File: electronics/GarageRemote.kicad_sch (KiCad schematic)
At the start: 33 parts, among them J1 CC1101 Module, J2 SERIAL, J3 ICSP, U1 TXS0108EPW, U2 ATmega328P-A, U3 MAX7060ATGT, Y1 16MHz, Y2 14.318MHz

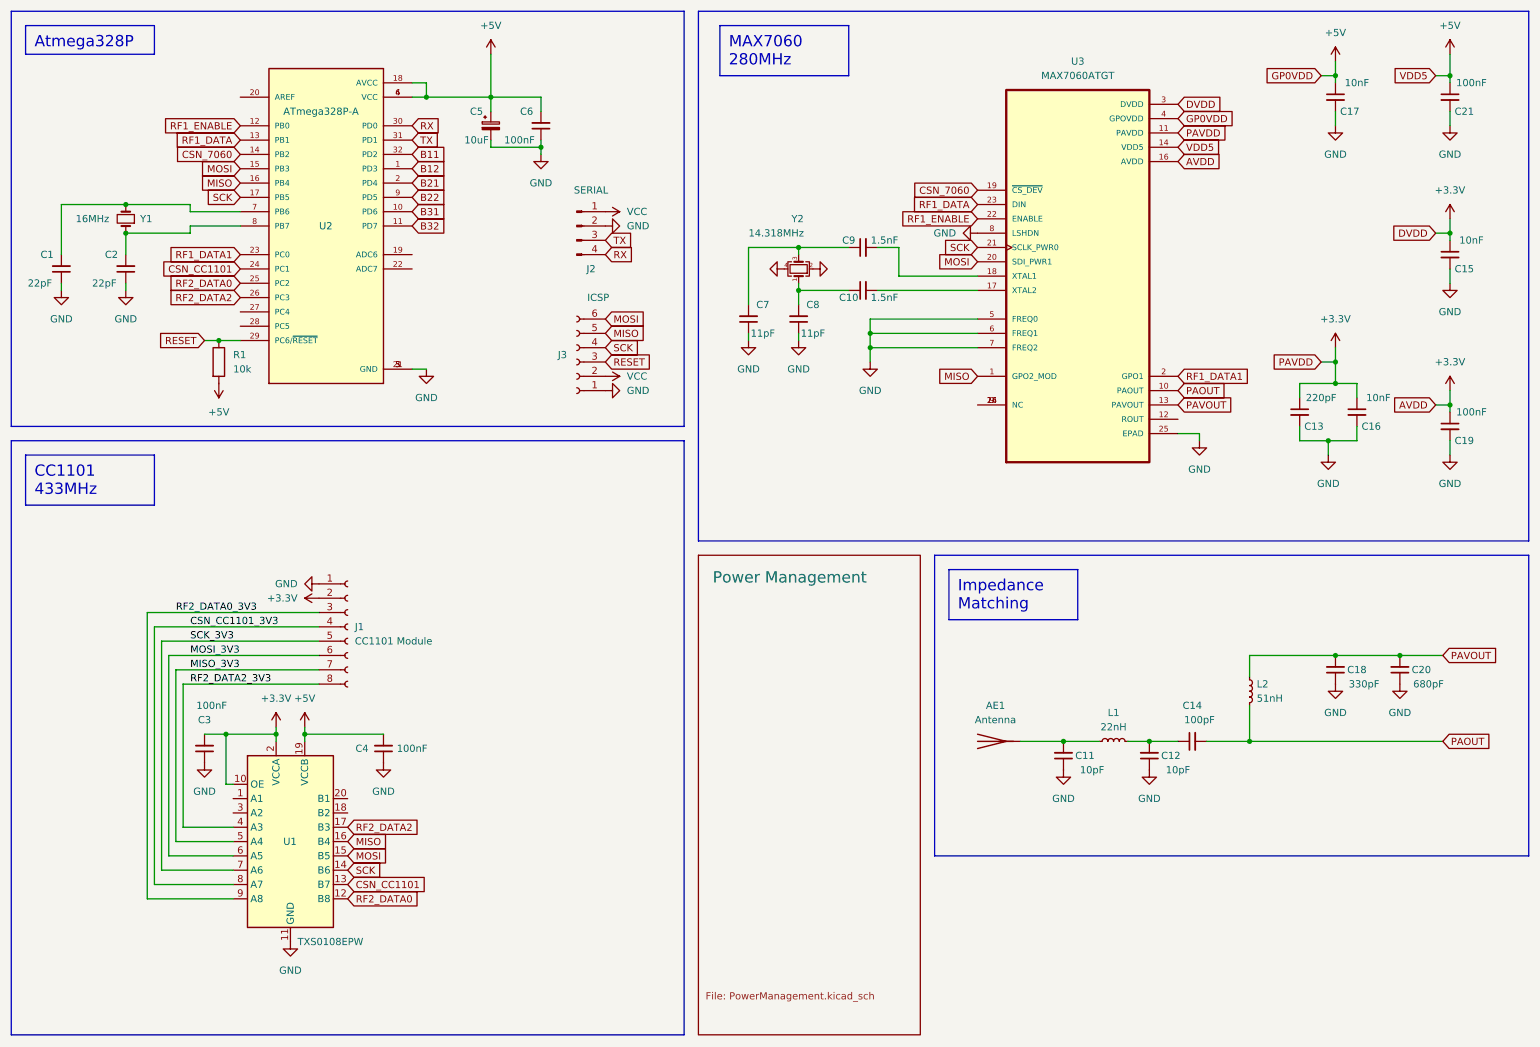
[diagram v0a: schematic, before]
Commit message: Fix & simplify schematic
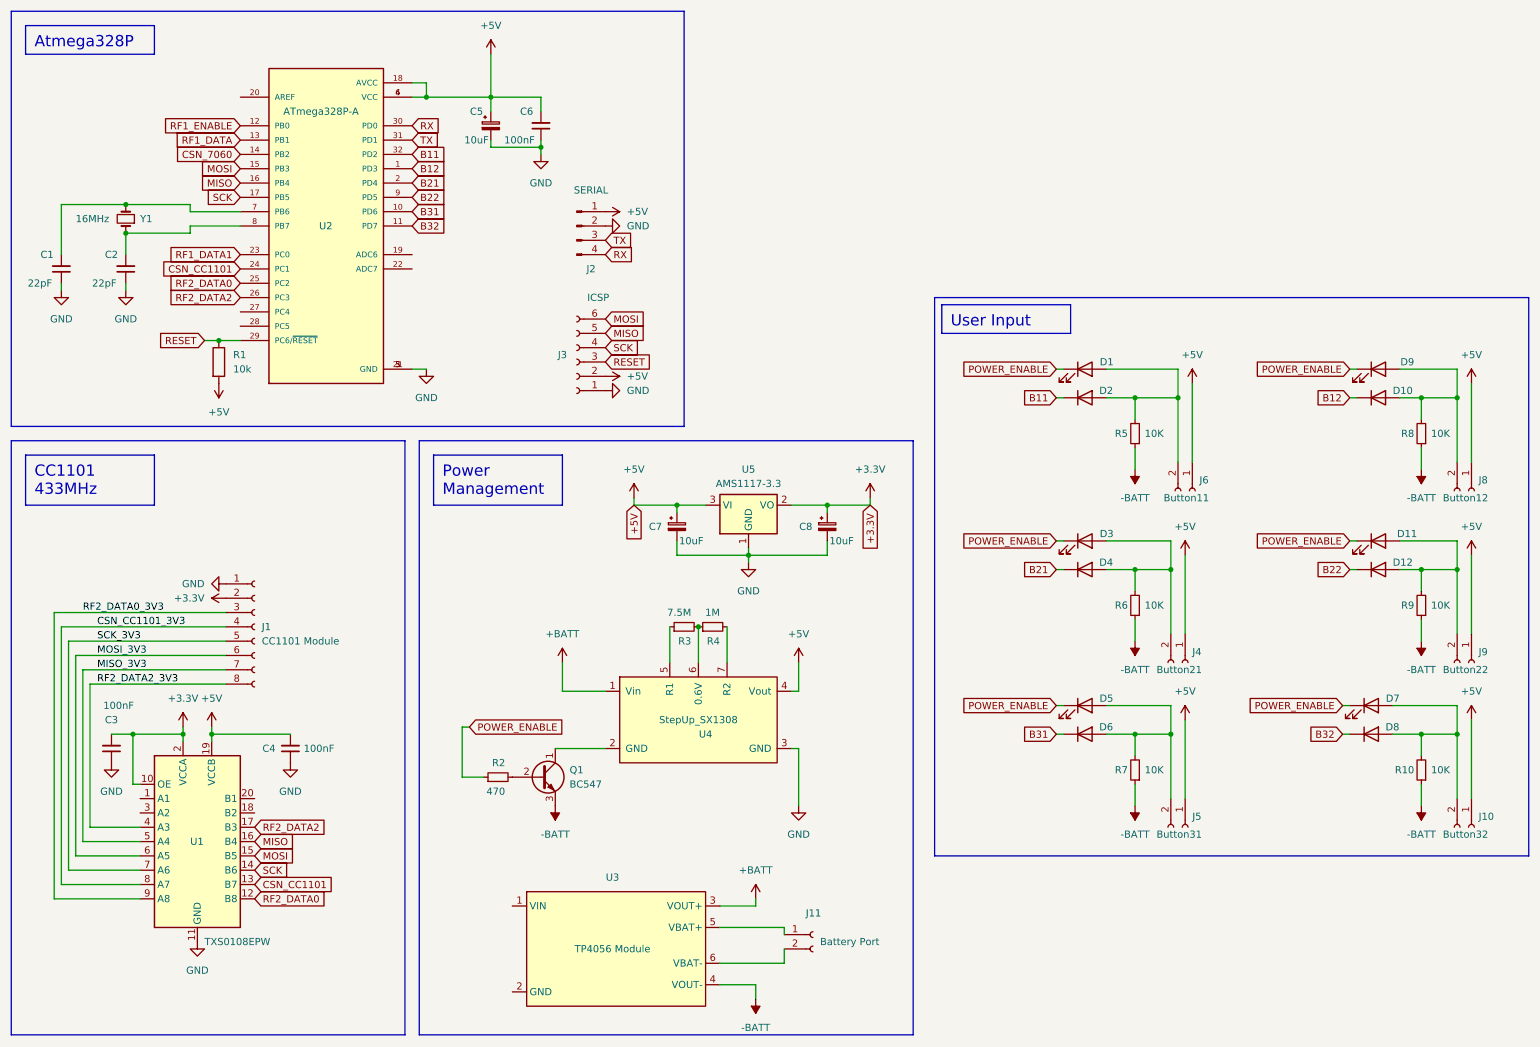
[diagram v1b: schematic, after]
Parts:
- removed AE1: Antenna, AA_Footprints:SMA-J-P-X-ST-EM1_EdgeMount, symbol Device:Antenna
- removed C10, C9: 1.5nF, Capacitor_SMD:C_0805_2012Metric_Pad1.18x1.45mm_HandSolder, symbol Device:C_Small
- removed C11, C12: 10pF, Capacitor_SMD:C_0805_2012Metric_Pad1.18x1.45mm_HandSolder, symbol Device:C_Small
- removed C13: 220pF, Capacitor_SMD:C_0805_2012Metric_Pad1.18x1.45mm_HandSolder, symbol Device:C_Small
- removed C14: 100pF, Capacitor_SMD:C_0805_2012Metric_Pad1.18x1.45mm_HandSolder, symbol Device:C_Small
- removed C15, C16, C17: 10nF, Capacitor_SMD:C_0805_2012Metric_Pad1.18x1.45mm_HandSolder, symbol Device:C_Small
- removed C18: 330pF, Capacitor_SMD:C_0805_2012Metric_Pad1.18x1.45mm_HandSolder, symbol Device:C_Small
- removed C19, C21: 100nF, Capacitor_SMD:C_1210_3225Metric_Pad1.33x2.70mm_HandSolder, symbol Device:C_Small
- removed C20: 680pF, Capacitor_SMD:C_0805_2012Metric_Pad1.18x1.45mm_HandSolder, symbol Device:C_Small
- removed C7, C8: 11pF, Capacitor_SMD:C_0805_2012Metric_Pad1.18x1.45mm_HandSolder, symbol Device:C_Small
- removed L1: 22nH, Inductor_SMD:L_0805_2012Metric_Pad1.15x1.40mm_HandSolder, symbol Device:L_Small
- removed L2: 51nH, Inductor_SMD:L_0805_2012Metric_Pad1.15x1.40mm_HandSolder, symbol Device:L_Small
- removed U3: MAX7060ATGT, AA_Footprints:MAX7060-TQFN24, symbol MAX7060ATGT:MAX7060ATGT
- removed Y2: 14.318MHz, Crystal:Crystal_SMD_Abracon_ABM8G-4Pin_3.2x2.5mm, symbol Device:Crystal_GND24_Small
- added C7, C8: 10uF, Capacitor_SMD:CP_Elec_6.3x4.9, symbol Device:C_Polarized_Small
- added D1, D11, D3, D5, D7, D9: LED, LED_SMD:LED_1206_3216Metric_Pad1.42x1.75mm_HandSolder, symbol Device:LED
- added D10, D12, D2, D4, D6, D8: 1N4001, Diode_SMD:D_SMA_Handsoldering, symbol Diode:1N4001
- added J10: Button32, AA_Footprints:4.5mm switch, symbol Connector:Conn_01x02_Socket
- added J11: Battery Port, Connector_JST:JST_PH_B2B-PH-K_1x02_P2.00mm_Vertical, symbol Connector:Conn_01x02_Socket
- added J4: Button21, AA_Footprints:4.5mm switch, symbol Connector:Conn_01x02_Socket
- added J5: Button31, AA_Footprints:4.5mm switch, symbol Connector:Conn_01x02_Socket
- added J6: Button11, AA_Footprints:4.5mm switch, symbol Connector:Conn_01x02_Socket
- added J8: Button12, AA_Footprints:4.5mm switch, symbol Connector:Conn_01x02_Socket
- added J9: Button22, AA_Footprints:4.5mm switch, symbol Connector:Conn_01x02_Socket
- added Q1: BC547, AA_Footprints:SOT-23-3-BC, symbol Transistor_BJT:BC547
- added R10, R5, R6, R7, R8, R9: 10K, Resistor_SMD:R_1206_3216Metric_Pad1.30x1.75mm_HandSolder, symbol Device:R_Small
- added R2: 470, Resistor_SMD:R_1206_3216Metric_Pad1.30x1.75mm_HandSolder, symbol Device:R_Small
- added R3: 7.5M, Resistor_SMD:R_0805_2012Metric_Pad1.20x1.40mm_HandSolder, symbol Device:R_Small
- added R4: 1M, Resistor_SMD:R_0805_2012Metric_Pad1.20x1.40mm_HandSolder, symbol Device:R_Small
- added U3: TP4056 Module, AA_Footprints:TP4056-Module, symbol 00_Symbols:TP4056_Module
- added U4: StepUp_SX1308, AA_Footprints:StepUp_SX1308, symbol 00_Symbols:StepUp_SX1308
- added U5: AMS1117-3.3, Package_TO_SOT_SMD:SOT-223-3_TabPin2, symbol Regulator_Linear:AMS1117-3.3
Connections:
- net VCC is gone; now on net +5V: J2.1 (Pin_1), J3.2 (Pin_2)
- net +3.3V: now also C8.1, U5.2 (VO)
- net +5V: now also C7.1, J10.1 (Pin_1), J4.1 (Pin_1), J5.1 (Pin_1), J6.1 (Pin_1), J8.1 (Pin_1), J9.1 (Pin_1), U4.4 (Vout), U5.3 (VI)
- net B11: now also D2.1 (K)
- net B12: now also D10.1 (K)
- net B21: now also D4.1 (K)
- net B22: now also D12.1 (K)
- net B31: now also D6.1 (K)
- net B32: now also D8.1 (K)
- net GND: now also C7.2, C8.2, U4.3 (GND), U5.1 (GND)
- new net: D5.2 (A), D6.2 (A), J5.2 (Pin_2), R7.2
- new net: D1.2 (A), D2.2 (A), J6.2 (Pin_2), R5.2
- new net: D3.2 (A), D4.2 (A), J4.2 (Pin_2), R6.2
- new net: D7.2 (A), D8.2 (A), J10.2 (Pin_2), R10.2
- new net: D11.2 (A), D12.2 (A), J9.2 (Pin_2), R9.2
- new net: J11.1 (Pin_1), U3.5 (VBAT+)
- new net: J11.2 (Pin_2), U3.6 (VBAT-)
- new net: D10.2 (A), D9.2 (A), J8.2 (Pin_2), R8.2
- new net: Q1.2 (B), R2.2
- new net: R3.1, U4.5 (R1)
- new net: R3.2, R4.1, U4.6 (0.6V)
- new net: Q1.1 (C), U4.2 (GND)
- new net: R4.2, U4.7 (R2)
- new net +BATT: U3.3 (VOUT+), U4.1 (Vin)
- new net -BATT: Q1.3 (E), R10.1, R5.1, R6.1, R7.1, R8.1, R9.1, U3.4 (VOUT-)
- new net POWER_ENABLE: D1.1 (K), D11.1 (K), D3.1 (K), D5.1 (K), D7.1 (K), D9.1 (K), R2.1
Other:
- removed sheet Power Management
- moved on the sheet: C3, C4, J1, U1
